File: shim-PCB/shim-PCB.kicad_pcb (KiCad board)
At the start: 2 copper layers, 67.5 x 95.4 mm, 25 parts, among them J1 ROMI-Encoder, J10 LineSensor, J11 LineSensor, J12 SPI, J13 Ultrasonic., J14 THING, J15 THING, J16 Conn_01x02_Female, J17 i2c, J2 ROMI-Encoder, J3 Conn_01x19_Female, J4 ServoAnalog, J5 Conn_01x19_Female, J6 Conn_01x19_Female, J7 ROMI, J8 ROMI, J9 Conn_01x19_Female

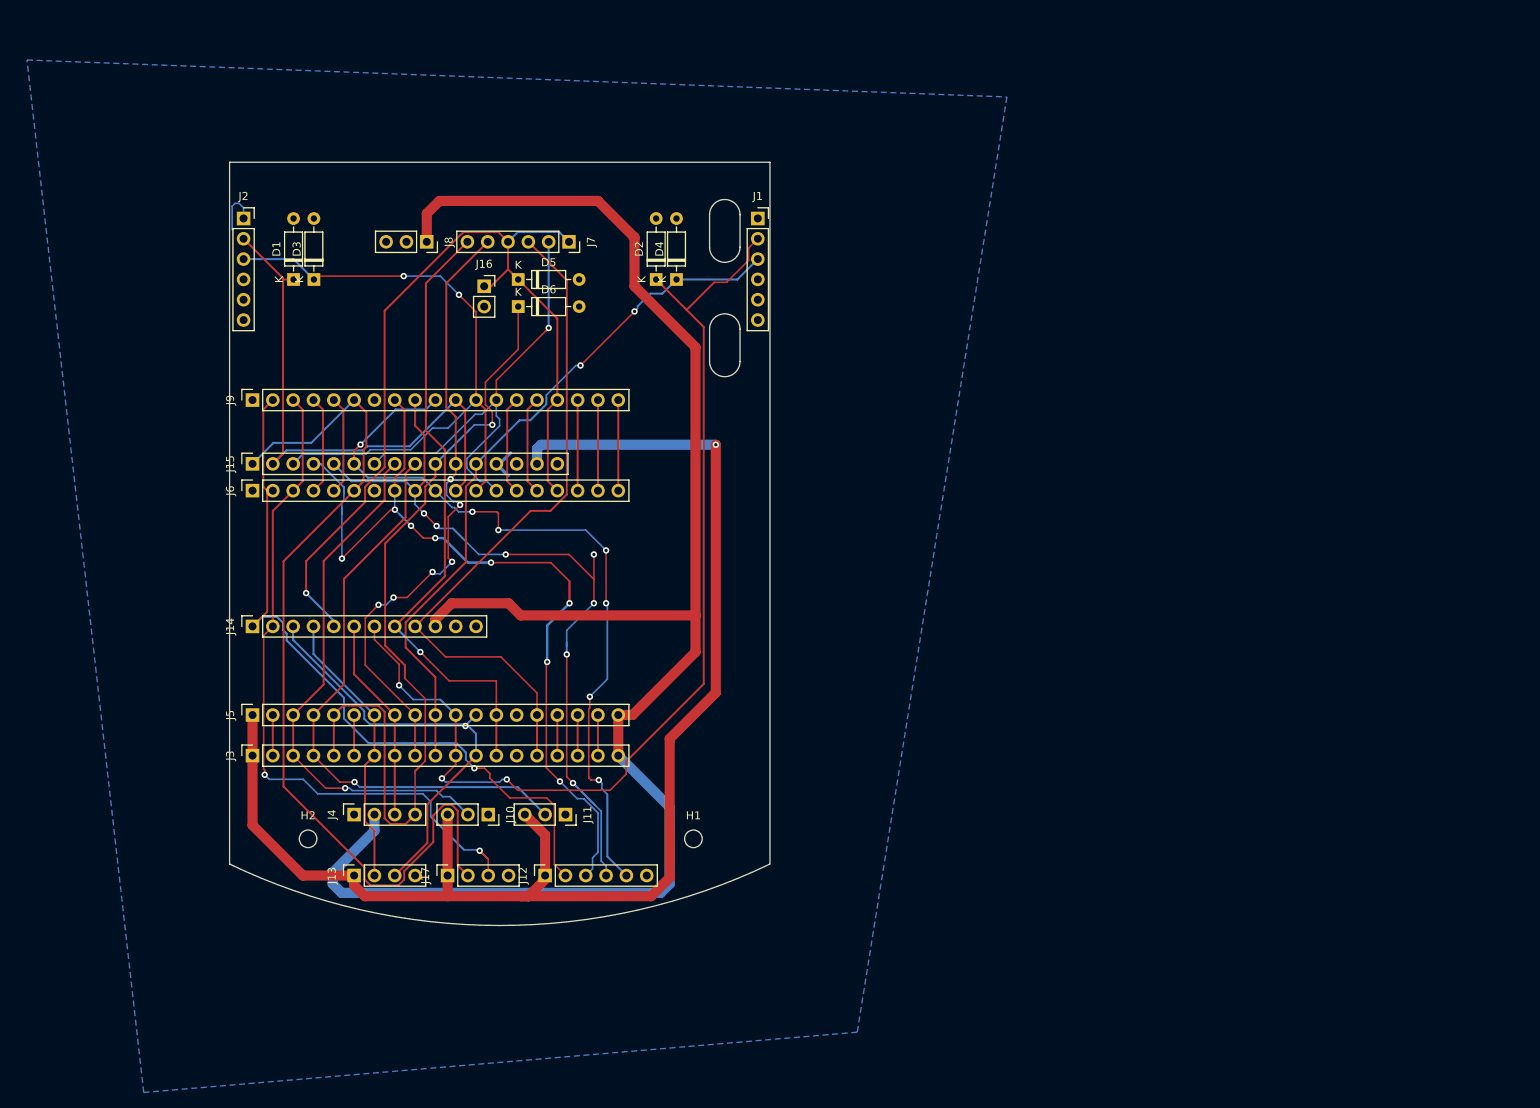
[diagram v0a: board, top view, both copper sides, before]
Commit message: Switched to 4 layer. Disconnected flash pins.
Resolved #15
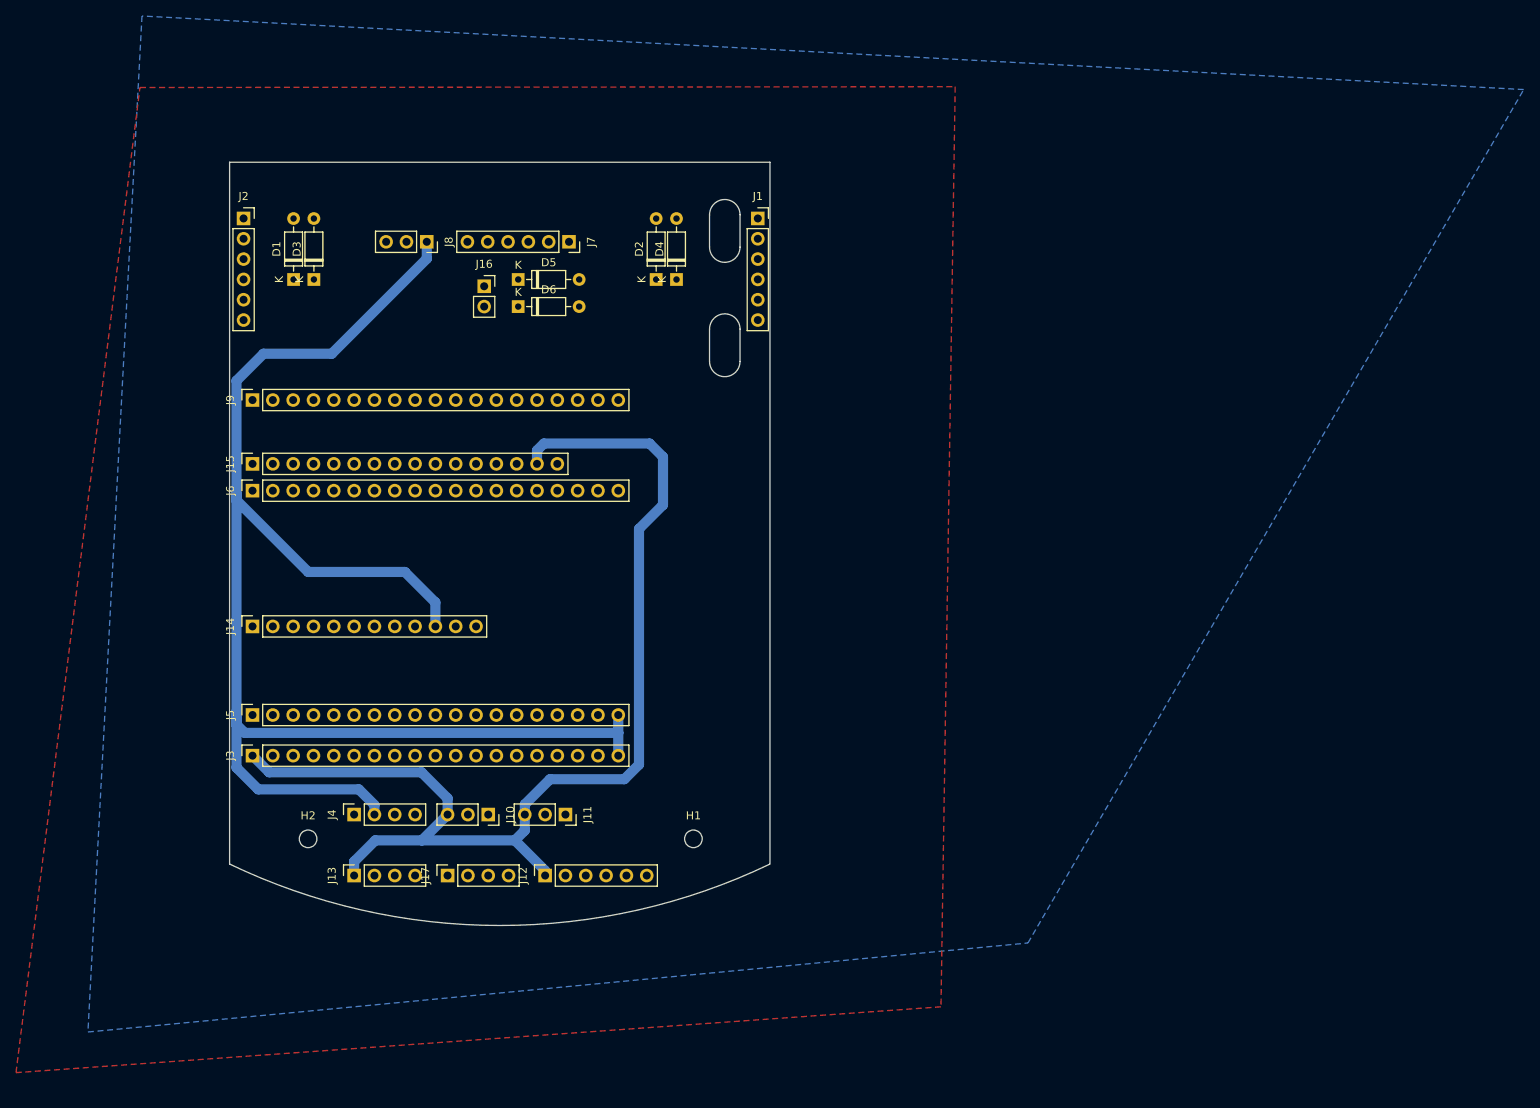
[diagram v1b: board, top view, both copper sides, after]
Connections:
- J3 pad 16: GPIO9 -> Net-(J3-Pad16)
- J3 pad 17: GPIO10 -> Net-(J3-Pad17)
- J3 pad 18: GPIO11 -> Net-(J3-Pad18)
- J5 pad 16: GPIO9 -> Net-(J5-Pad16)
- J5 pad 17: GPIO10 -> Net-(J5-Pad17)
- J5 pad 18: GPIO11 -> Net-(J5-Pad18)
- J6 pad 17: GPIO8 -> Net-(J6-Pad17)
- J6 pad 18: GPIO7 -> Net-(J6-Pad18)
- J6 pad 19: GPIO6 -> Net-(J6-Pad19)
- J9 pad 17: GPIO8 -> Net-(J9-Pad17)
- J9 pad 18: GPIO7 -> Net-(J9-Pad18)
- J9 pad 19: GPIO6 -> Net-(J9-Pad19)
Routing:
- net +5V: track 212.4 -> 189.7 mm
- net GPIO34: track 106.1 -> 84.2 mm, vias 1 -> 0
- net +3V3: track 175.6 -> 154.3 mm, vias 1 -> 0
- net GPIO15: track 112.1 -> 91.0 mm, vias 1 -> 0
- net GPIO19: track 105.9 -> 85.2 mm, vias 8 -> 0
- net GPIO21: track 112.7 -> 95.4 mm
- net GPIO27: track 132.4 -> 115.6 mm, vias 3 -> 0
- net GPIO18: track 99.7 -> 83.8 mm, vias 7 -> 0
- net GPIO16: track 81.6 -> 67.5 mm, vias 2 -> 0
- net GPIO5: track 95.8 -> 83.8 mm, vias 7 -> 0
- net GPIO8: track 11.3 -> 0.00 mm
- net GPIO7: track 11.3 -> 0.00 mm
- net GPIO6: track 11.3 -> 0.00 mm
- net GPIO25: track 78.8 -> 68.0 mm, vias 6 -> 0
- net GND: track 10.5 -> 0.00 mm
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- added copper zone on F.Cu, net GND
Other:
- copper layers 2 -> 4

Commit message: Updated Silk and finished board.
#16
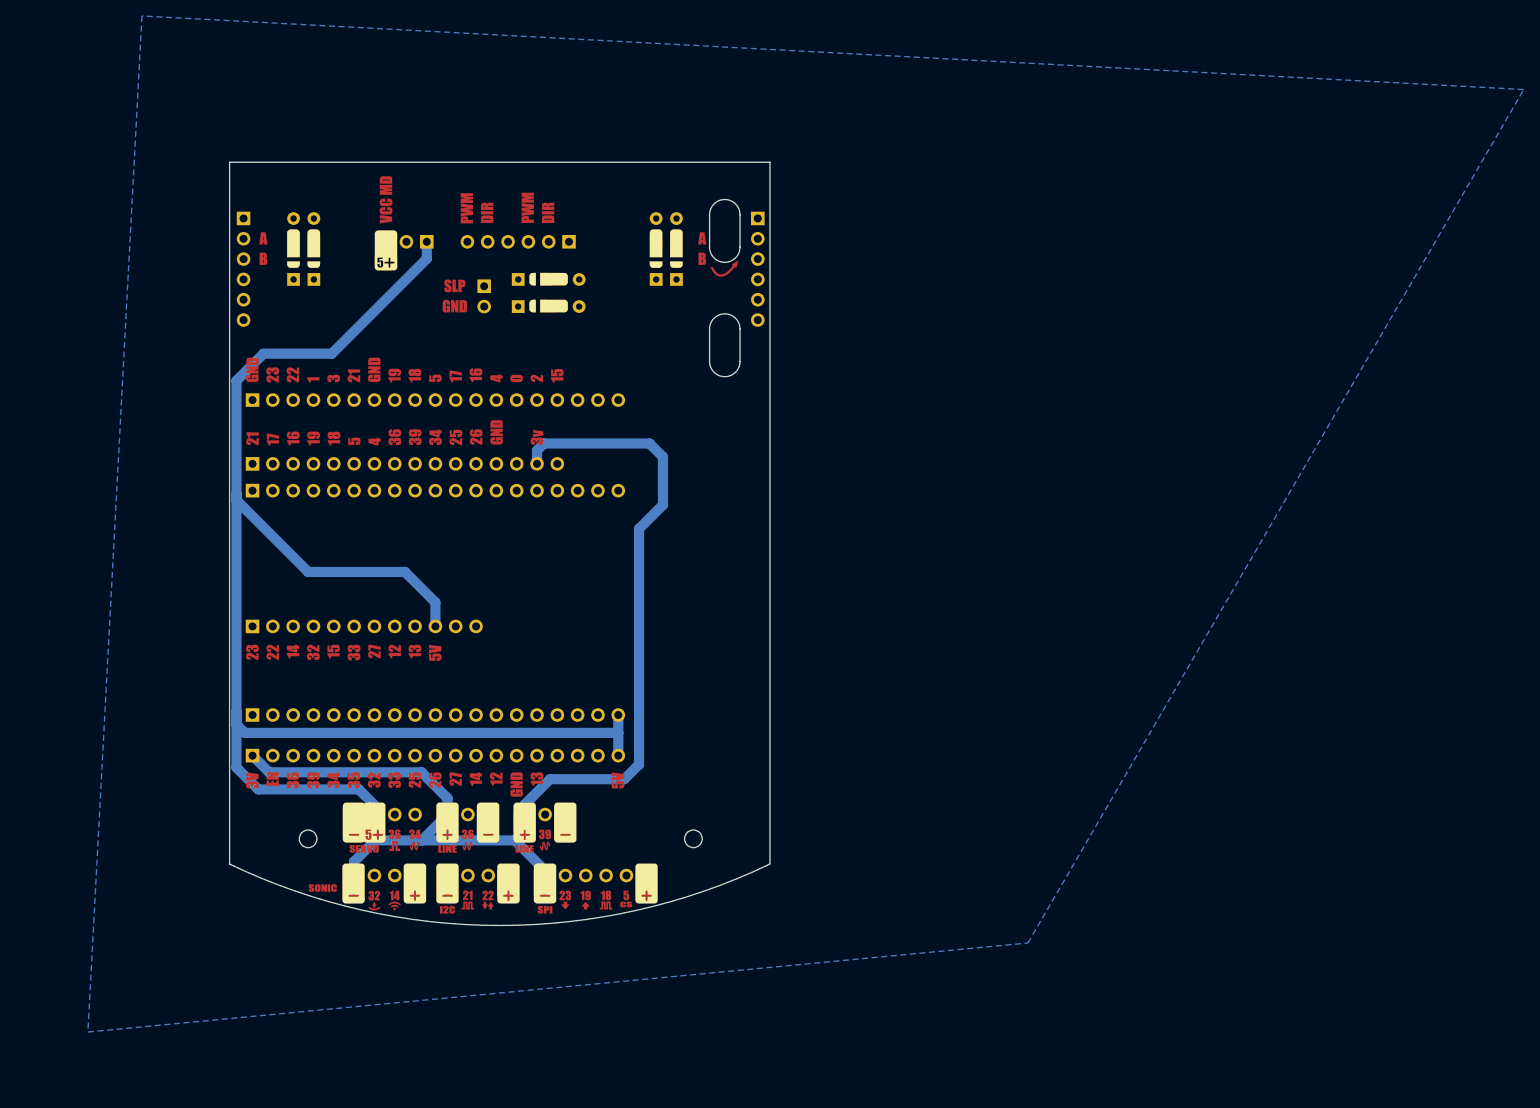
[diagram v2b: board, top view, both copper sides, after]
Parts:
- added Ref**: Val**, shim-PCB:silkscreen, F.Cu at (153.5, 95.7)
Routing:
- removed copper zone on F.Cu, net GND

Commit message: Added board label.
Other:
- board text added: "1001 Romi Shim V1 Alex Camilo"
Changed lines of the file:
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@@
   (general
     (thickness 1.6)
-    (drawings 159)
+    (drawings 162)
     (tracks 324)
     (zones 0)
@@
   (page A4)
   (layers
-    (0 F.Cu signal hide)
+    (0 F.Cu signal)
     (1 In1.Cu signal hide)
     (2 In2.Cu signal hide)
@@
     (visible_elements 7FFFFFFF)
     (pcbplotparams
-      (layerselection 0x08080_7ffffffe)
+      (layerselection 0x010f0_ffffffff)
       (usegerberextensions false)
       (usegerberattributes false)
@@
       (padsonsilk false)
       (subtractmaskfromsilk false)
-      (outputformat 5)
+      (outputformat 1)
       (mirror false)
       (drillshape 0)
       (scaleselection 1)
-      (outputdirectory "silkscreen-base"))
+      (outputdirectory "gerbers"))
   )
   (net 0 "")
@@
     (pad 1 np_thru_hole circle (at 0 0) (size 2.2 2.2) (drill 2.2) (layers *.Cu *.Mask))
   )
+  (gr_text "1001 Romi Shim V1       Alex Camilo" (at 172.72 99.06 90) (layer F.SilkS)
+    (effects (font (size 1.5 1.5) (thickness 0.3)))
+  )
+  (gr_line (start 107.878075 48.006) (end 175.425701 48.006) (layer Edge.Cuts) (width 0.05))
+  (gr_line (start 107.878075 135.724057) (end 107.878075 48.006) (layer Edge.Cuts) (width 0.05))
   (gr_circle (center 148.844 132.334) (end 149.494 132.334) (layer Dwgs.User) (width 0.05))
   (gr_circle (center 148.844 134.874) (end 149.494 134.874) (layer Dwgs.User) (width 0.05))

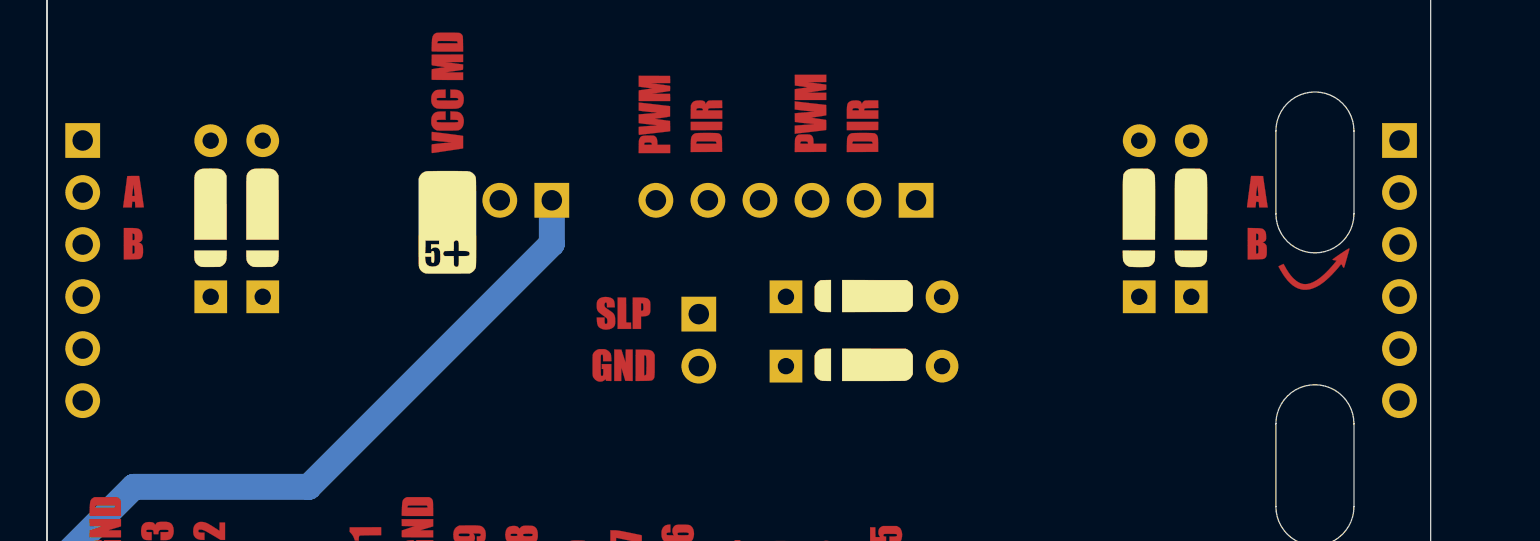
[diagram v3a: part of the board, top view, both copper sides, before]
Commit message: swapped right encoder
#24
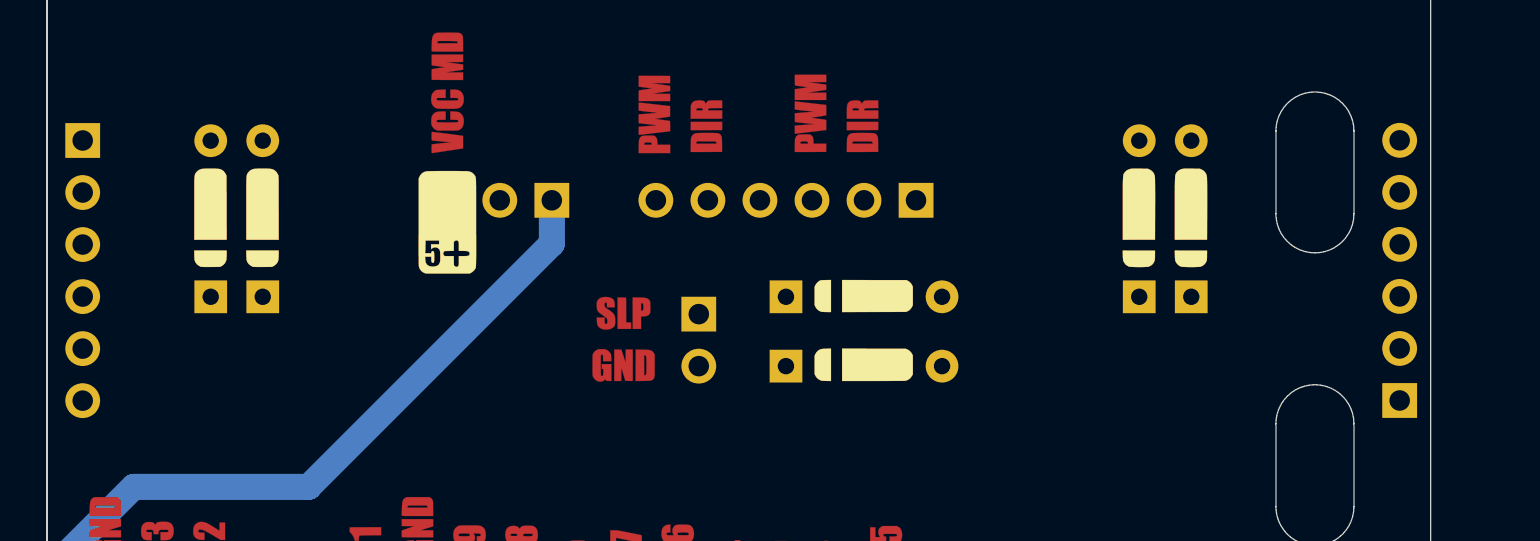
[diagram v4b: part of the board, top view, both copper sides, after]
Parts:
- moved J1 12.7 mm to (173.9, 67.7), turned to 180 degrees
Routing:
- net GPIO26: track 85.9 -> 90.8 mm
- net GPIO27: track 115.6 -> 113.6 mm
